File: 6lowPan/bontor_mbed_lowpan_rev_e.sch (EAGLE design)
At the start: 170 parts, among them IC1 SIM900, IC2 74HC595D, IC3 74HC595D, IC4 ADE7758RW, IC5 74HC595D, J1 U.FL, U2 W5500, X1 NX2520SA

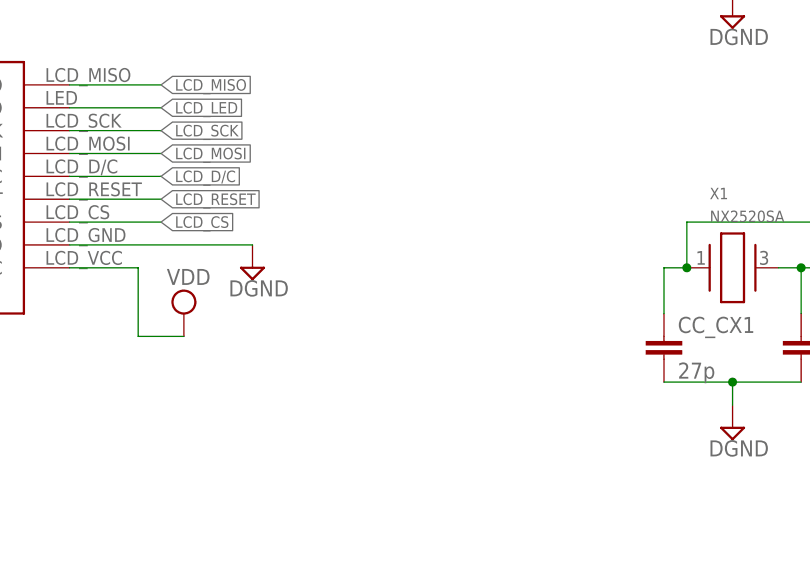
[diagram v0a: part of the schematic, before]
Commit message: update silkscreen and delete USB micro hole
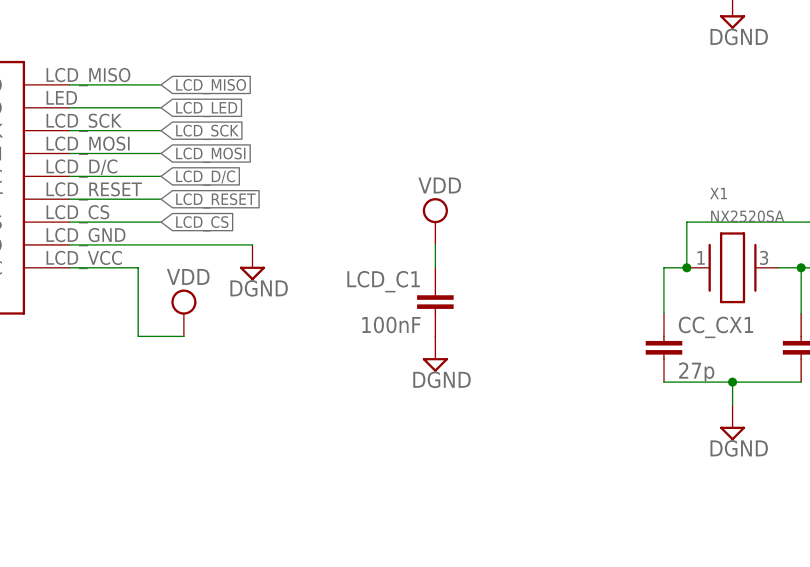
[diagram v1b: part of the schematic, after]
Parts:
- added LCD_C1: 100nF, rcl:C-EUC0603
- S1: device SparkFun-Electromechanical:TAC_SWITCHSMD -> SparkFun-Electromechanical:TAC_SWITCHPTH
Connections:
- net DGND: now also LCD_C1.2
- net VDD: now also LCD_C1.1
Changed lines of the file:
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@@
 <part name="PWR-SWT" library="rcl" deviceset="R-EU_" device="R0402"/>
 <part name="SUPPLY82" library="supply2" deviceset="VDD" device=""/>
-<part name="S1" library="SparkFun-Electromechanical" deviceset="TAC_SWITCH" device="SMD"/>
+<part name="S1" library="SparkFun-Electromechanical" deviceset="TAC_SWITCH" device="PTH"/>
 <part name="BAT1" library="SparkFun-Electromechanical" deviceset="BATTERY" device="12MM"/>
 <part name="STM-XTAL" library="SparkFun-FreqCtrl" deviceset="CRYSTAL" device="TC26H" value="32.768kHz"/>
@@
 <part name="SUPPLY132" library="supply2" deviceset="DGND" device=""/>
 <part name="U$17" library="DHT11" deviceset="DHT11" device=""/>
+<part name="LCD_C1" library="rcl" deviceset="C-EU" device="C0603" value="100nF"/>
+<part name="SUPPLY95" library="supply2" deviceset="VDD" device=""/>
+<part name="SUPPLY129" library="supply2" deviceset="DGND" device=""/>
 </parts>
 <sheets>
@@
 <instance part="SUPPLY132" gate="G$1" x="218.44" y="119.38"/>
 <instance part="U$17" gate="G$1" x="462.28" y="391.16" rot="R270"/>
+<instance part="LCD_C1" gate="G$1" x="469.9" y="76.2" rot="MR0"/>
+<instance part="SUPPLY95" gate="G$1" x="469.9" y="83.82"/>
+<instance part="SUPPLY129" gate="G$1" x="469.9" y="68.58"/>
 </instances>
 <busses>
@@
 <wire x1="218.44" y1="121.92" x2="213.36" y2="121.92" width="0.1524" layer="91"/>
 </segment>
+<segment>
+<pinref part="LCD_C1" gate="G$1" pin="2"/>
+<pinref part="SUPPLY129" gate="G$1" pin="DGND"/>
+</segment>
 </net>
 <net name="VDD" class="0">
@@
 <wire x1="566.42" y1="22.86" x2="568.96" y2="22.86" width="0.1524" layer="91"/>
 </segment>
+<segment>
+<pinref part="SUPPLY95" gate="G$1" pin="VDD"/>
+<pinref part="LCD_C1" gate="G$1" pin="1"/>
+<wire x1="469.9" y1="78.74" x2="469.9" y2="81.28" width="0.1524" layer="91"/>
+</segment>
 </net>
